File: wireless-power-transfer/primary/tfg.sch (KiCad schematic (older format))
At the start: 32 parts

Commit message: New version with changed interruptors, improved routing layout, fixed 3d designs and Wi-Fi module, among other minor changes
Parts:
- removed C? (x2): 0.1uF, symbol C_Small
- removed Cboot (x2): C_Small, symbol C_Small
- removed D? (x2): D, symbol D
- removed Q? (x4): IRLB8721PBF, TO_SOT_Packages_THT:TO-220_Vertical, symbol IRLB8721PBF
- removed U? (x2): IR2110, DIL14-1, symbol IR2110
- removed U?: PIC18F45K20-I/PT, QFP80P1200X1200X120-44N, symbol PIC18F45K20-I/PT
- removed U? (x2): Pickit3, symbol Pickit3
- removed U? (x2): AP111733, TO_SOT_Packages_SMD:SOT-223, symbol AP111733
- removed U? (x2): LM7815ACT, TO_SOT_Packages_THT:TO-220_Vertical, symbol LM7815ACT
- added 47uH1: L, Choke_SMD:Choke_SMD_12x12mm_h6mm, symbol L
- added C5, C6, C7: 10uF, Capacitors_SMD:C_1206_HandSoldering, symbol C
- added Cf1: 47nF, Capacitors_THT:C_Rect_L18.0mm_W5.0mm_P15.00mm_FKS3_FKP3, symbol C
- added Cf2: 22nF, Capacitors_THT:C_Rect_L13.0mm_W5.0mm_P10.00mm_FKS3_FKP3_MKS4, symbol C
- added Cr1: 150nF, Capacitors_THT:C_Rect_L7.2mm_W2.5mm_P5.00mm_FKS2_FKP2_MKS2_MKP2, symbol C
- added Cr2: 470nF, Capacitors_THT:C_Rect_L18.0mm_W11.0mm_P15.00mm_FKS3_FKP3, symbol C
- added F1: Fuse, Fuse_Holders_and_Fuses:Fuseholder5x20_horiz_SemiClosed_Casing10x25mm, symbol Fuse
- added J1: CONN_01X06, Pin_Headers:Pin_Header_Angled_1x06_Pitch2.54mm, symbol CONN_01X06
- added J2: Screw_Terminal_1x02, Connectors_Terminal_Blocks:TerminalBlock_Pheonix_MKDS1.5-2pol, symbol Screw_Terminal_1x02
- added J3: BARREL_JACK, Connectors:BARREL_JACK, symbol BARREL_JACK
- added SW_MANUAL1, SW_ON_OFF1, SW_POW1: SW_SPDT, componentes:SPDT_Toggle_Switch, symbol SW_SPDT
- added U4: R-78E15, componentes:r-78Exx, symbol R-78E3.3
- added U5: R-78E3.3, componentes:r-78Exx, symbol R-78E3.3
- added U6: XBEE_Wi-Fi, componentes:XBee_Wi-Fi, symbol XBEE_Wi-Fi
- C1, C2: renamed from C?; footprint (none) -> Capacitors_SMD:C_1206_HandSoldering
- Cboot1, Cboot2: renamed from Cboot?; value C_Small -> 0.47uF; footprint (none) -> Capacitors_SMD:C_1206_HandSoldering
- D1, D2: renamed from D?; footprint (none) -> Diodes_THT:D_DO-35_SOD27_P5.08mm_Vertical_AnodeUp
- Q1, Q2, Q3, Q4: renamed from Q?; footprint TO_SOT_Packages_THT:TO-220_Vertical -> TO_SOT_Packages_THT:TO-220-3_Vertical
- U1: renamed from U?; footprint QFP80P1200X1200X120-44N -> componentes:PIC18F45K20
- U2, U3: renamed from U?; footprint DIL14-1 -> Housings_DIP:DIP-14_W7.62mm
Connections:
- net labels removed: +24V, Earth, GND
- wire segments 104 -> 176
- no-connect marks 0 -> 42

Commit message: New version with changed interruptors, improved routing layout, fixed 3d designs and Wi-Fi module, among other minor changes.
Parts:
- U1: footprint componentes:PIC18F45K20 -> componentesGIT:PIC18F45K20
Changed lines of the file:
@@
 F 0 "U1" H 4664 7309 50  0000 L BNN
 F 1 "PIC18F45K20-I/PT" H 4529 3716 50  0000 L BNN
-F 2 "componentes:PIC18F45K20" H 4850 5650 50  0001 L BNN
+F 2 "componentesGIT:PIC18F45K20" H 4850 5650 50  0001 L BNN
 F 3 "2.16 USD" H 4850 5650 50  0001 L BNN
 F 4 "TQFP-44 10x10x1mm Tray%2C 32KB%2C Flash%2C 1536bytes-RAM%2C 36I/O%2C 8-Bit nanoWatt" H 4850 5650 50  0001 L BNN "Description"

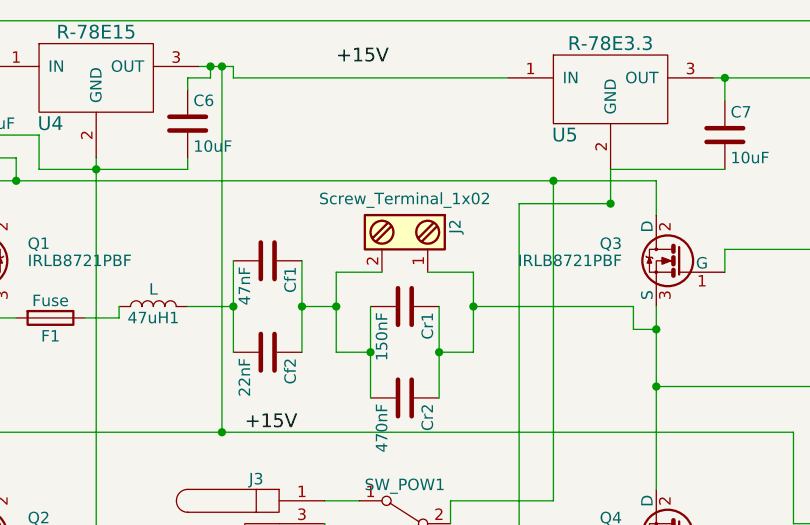
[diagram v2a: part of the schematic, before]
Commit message: Orientation of the primary coil connector fixed.
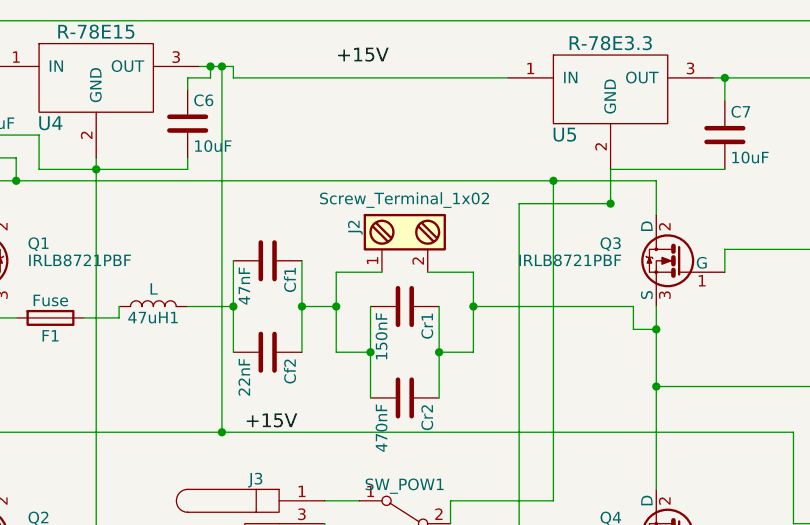
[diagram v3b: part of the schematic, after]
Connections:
- net at Cboot2.2, Cr1.1, Cr2.1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: now also J2.2; no longer J2.1
- net at Cf1.1, Cf2.1, Cr1.2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: now also J2.1; no longer J2.2
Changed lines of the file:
@@
 F 3 "" H 6075 1450 50  0001 C CNN
 	1    6100 1450
-	0    1    1    0
+	0    -1   1    0
 $EndComp
 Wire Wire Line

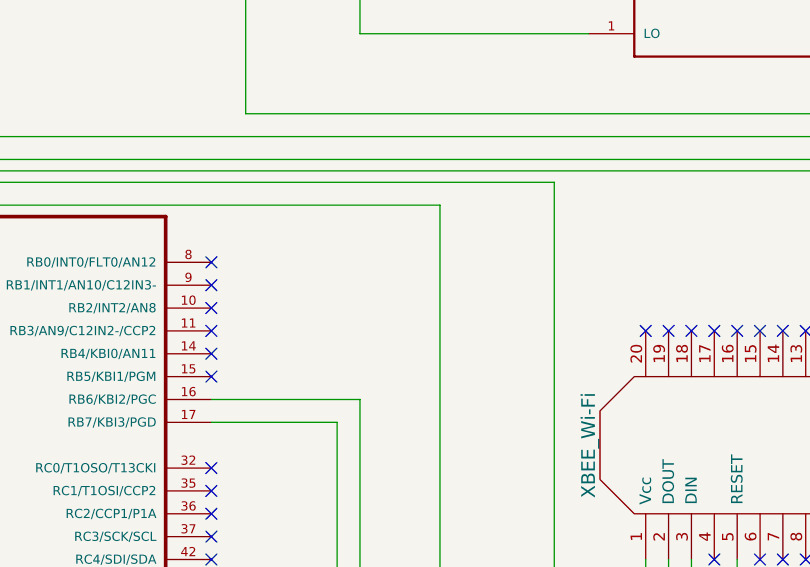
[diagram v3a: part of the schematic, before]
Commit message: LEDs for power and charging indication added.
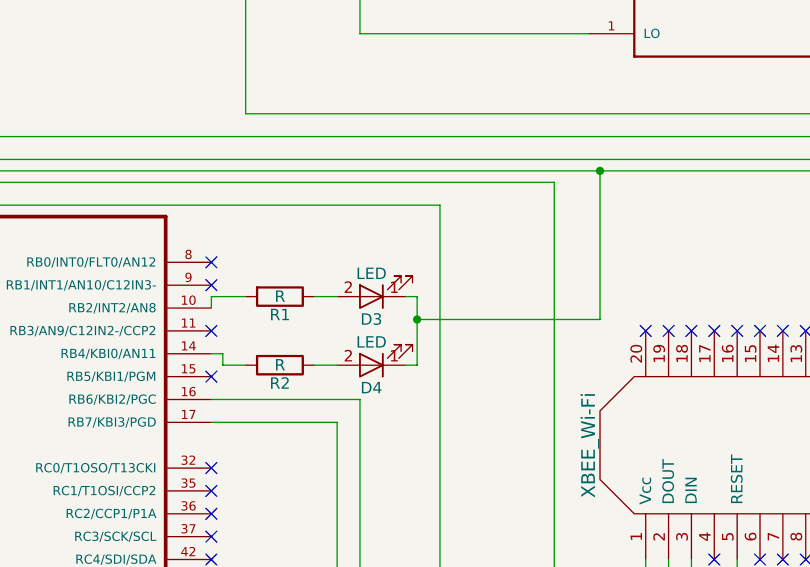
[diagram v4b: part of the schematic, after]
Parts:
- added D3, D4: LED, LEDs:LED_D3.0mm, symbol LED
- added R1, R2: R, Resistors_SMD:R_1206_HandSoldering, symbol R
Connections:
- net at C1.2, C2.2, C5.2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: now also D3.1 (K), D4.1 (K)
- net at U1.10 (RB2/INT2/AN8): now also R1.2
- net at U1.14 (RB4/KBI0/AN11): now also R2.2
- new net: D3.2 (A), R1.1
- new net: D4.2 (A), R2.1
- no-connect marks 42 -> 40
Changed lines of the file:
@@
 NoConn ~ 2850 6350
 NoConn ~ 2850 6450
-NoConn ~ 6850 4550
 NoConn ~ 6850 4650
-NoConn ~ 6850 4750
 NoConn ~ 6850 4850
 NoConn ~ 6850 5250
@@
 NoConn ~ 8850 4650
 NoConn ~ 8750 4650
+$Comp
+L LED D3
+U 1 1 59E8E0C4
+P 7550 4500
+F 0 "D3" H 7550 4600 50  0000 C CNN
+F 1 "LED" H 7550 4400 50  0000 C CNN
+F 2 "LEDs:LED_D3.0mm" H 7550 4500 50  0001 C CNN
+F 3 "" H 7550 4500 50  0001 C CNN
+	1    7550 4500
+	-1   0    0    1
+$EndComp
+$Comp
+L LED D4
+U 1 1 59E8E153
+P 7550 4800
+F 0 "D4" H 7550 4900 50  0000 C CNN
+F 1 "LED" H 7550 4700 50  0000 C CNN
+F 2 "LEDs:LED_D3.0mm" H 7550 4800 50  0001 C CNN
+F 3 "" H 7550 4800 50  0001 C CNN
+	1    7550 4800
+	-1   0    0    1
+$EndComp
+Wire Wire Line
+	6850 4550 6850 4500
+Wire Wire Line
+	6850 4750 6900 4750
+Wire Wire Line
+	6900 4750 6900 4800
+$Comp
+L R R1
+U 1 1 59E8E857
+P 7150 4500
+F 0 "R1" V 7230 4500 50  0000 C CNN
+F 1 "R" V 7150 4500 50  0000 C CNN
+F 2 "Resistors_SMD:R_1206_HandSoldering" V 7080 4500 50  0001 C CNN
+F 3 "" H 7150 4500 50  0001 C CNN
+	1    7150 4500
+	0    1    1    0
+$EndComp
+$Comp
+L R R2
+U 1 1 59E8E904
+P 7150 4800
+F 0 "R2" V 7230 4800 50  0000 C CNN
+F 1 "R" V 7150 4800 50  0000 C CNN
+F 2 "Resistors_SMD:R_1206_HandSoldering" V 7080 4800 50  0001 C CNN
+F 3 "" H 7150 4800 50  0001 C CNN
+	1    7150 4800
+	0    1    1    0
+$EndComp
+Wire Wire Line
+	7750 4800 7750 4500
+Wire Wire Line
+	7750 4600 8550 4600
+Wire Wire Line
+	8550 4600 8550 3950
+Connection ~ 8550 3950
+Connection ~ 7750 4600
+Wire Wire Line
+	6850 4500 7000 4500
+Wire Wire Line
+	7300 4500 7400 4500
+Wire Wire Line
+	7400 4800 7300 4800
+Wire Wire Line
+	6900 4800 7000 4800
+Wire Wire Line
+	7750 4500 7700 4500
+Wire Wire Line
+	7700 4800 7750 4800
 $EndSCHEMATC

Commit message: fixed MOSFET sizes and some excessively small pads.
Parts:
- Q1, Q2, Q3, Q4: footprint TO_SOT_Packages_THT:TO-220-3_Vertical -> componentesGIT:TO-247AC
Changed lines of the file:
@@
 LIBS:switches
 LIBS:xbee_wi-fi
+LIBS:irlb8721pbf
 LIBS:tfg-cache
 EELAYER 25 0
@@
 	1    2150 2350
 	1    0    0    -1
-$EndComp
-$Comp
-L IRLB8721PBF Q1
-U 1 1 592C7EC3
-P 4200 1600
-F 0 "Q1" H 4450 1675 50  0000 L CNN
-F 1 "IRLB8721PBF" H 4450 1600 50  0000 L CNN
-F 2 "TO_SOT_Packages_THT:TO-220-3_Vertical" H 4450 1525 50  0001 L CIN
-F 3 "" H 4200 1600 50  0001 L CNN
-	1    4200 1600
-	1    0    0    -1
-$EndComp
-$Comp
-L IRLB8721PBF Q2
-U 1 1 592C7EC4
-P 4200 2800
-F 0 "Q2" H 4450 2875 50  0000 L CNN
-F 1 "IRLB8721PBF" H 4450 2800 50  0000 L CNN
-F 2 "TO_SOT_Packages_THT:TO-220-3_Vertical" H 4450 2725 50  0001 L CIN
-F 3 "" H 4200 2800 50  0001 L CNN
-	1    4200 2800
-	1    0    0    -1
-$EndComp
-$Comp
-L IRLB8721PBF Q3
-U 1 1 592C7EC5
-P 7300 1600
-F 0 "Q3" H 7550 1675 50  0000 L CNN
-F 1 "IRLB8721PBF" H 7550 1600 50  0000 L CNN
-F 2 "TO_SOT_Packages_THT:TO-220-3_Vertical" H 7550 1525 50  0001 L CIN
-F 3 "" H 7300 1600 50  0001 L CNN
-	1    7300 1600
-	-1   0    0    -1
-$EndComp
-$Comp
-L IRLB8721PBF Q4
-U 1 1 592C7EC6
-P 7300 2800
-F 0 "Q4" H 7550 2875 50  0000 L CNN
-F 1 "IRLB8721PBF" H 7550 2800 50  0000 L CNN
-F 2 "TO_SOT_Packages_THT:TO-220-3_Vertical" H 7550 2725 50  0001 L CIN
-F 3 "" H 7300 2800 50  0001 L CNN
-	1    7300 2800
-	-1   0    0    -1
 $EndComp
 $Comp
@@
 Wire Wire Line
 	7700 4800 7750 4800
+$Comp
+L IRLB8721PBF Q1
+U 1 1 59E9A11A
+P 4200 1600
+F 0 "Q1" H 4450 1675 50  0000 L CNN
+F 1 "IRLB8721PBF" H 4450 1600 50  0000 L CNN
+F 2 "componentesGIT:TO-247AC" H 4450 1525 50  0001 L CIN
+F 3 "" H 4200 1600 50  0001 L CNN
+	1    4200 1600
+	1    0    0    -1
+$EndComp
+$Comp
+L IRLB8721PBF Q2
+U 1 1 59E9A26F
+P 4200 2800
+F 0 "Q2" H 4450 2875 50  0000 L CNN
+F 1 "IRLB8721PBF" H 4450 2800 50  0000 L CNN
+F 2 "componentesGIT:TO-247AC" H 4450 2725 50  0001 L CIN
+F 3 "" H 4200 2800 50  0001 L CNN
+	1    4200 2800
+	1    0    0    -1
+$EndComp
+$Comp
+L IRLB8721PBF Q3
+U 1 1 59E9A30C
+P 7300 1600
+F 0 "Q3" H 7550 1675 50  0000 L CNN
+F 1 "IRLB8721PBF" H 7550 1600 50  0000 L CNN
+F 2 "componentesGIT:TO-247AC" H 7550 1525 50  0001 L CIN
+F 3 "" H 7300 1600 50  0001 L CNN
+	1    7300 1600
+	-1   0    0    -1
+$EndComp
+$Comp
+L IRLB8721PBF Q4
+U 1 1 59E9A4FE
+P 7300 2800
+F 0 "Q4" H 7550 2875 50  0000 L CNN
+F 1 "IRLB8721PBF" H 7550 2800 50  0000 L CNN
+F 2 "componentesGIT:TO-247AC" H 7550 2725 50  0001 L CIN
+F 3 "" H 7300 2800 50  0001 L CNN
+	1    7300 2800
+	-1   0    0    -1
+$EndComp
 $EndSCHEMATC
